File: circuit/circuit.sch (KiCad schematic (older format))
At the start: 4 parts

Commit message: Minor changes
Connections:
- wire segments 11 -> 15
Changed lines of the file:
@@
 EESchema Schematic File Version 4
+LIBS:circuit-cache
 EELAYER 26 0
 EELAYER END
@@
 L pspice:R R1
 U 1 1 5A75EF1D
-P 4700 2450
-F 0 "R1" H 4768 2496 50  0000 L CNN
-F 1 "R" H 4768 2405 50  0000 L CNN
-F 2 "" H 4700 2450 50  0001 C CNN
-F 3 "" H 4700 2450 50  0001 C CNN
-	1    4700 2450
+P 4900 3250
+F 0 "R1" H 4968 3296 50  0000 L CNN
+F 1 "R" H 4968 3205 50  0000 L CNN
+F 2 "" H 4900 3250 50  0001 C CNN
+F 3 "" H 4900 3250 50  0001 C CNN
+	1    4900 3250
 	1    0    0    -1
 $EndComp
@@
 L pspice:R R2
 U 1 1 5A75EF72
-P 5150 2450
-F 0 "R2" H 5218 2496 50  0000 L CNN
-F 1 "R" H 5218 2405 50  0000 L CNN
-F 2 "" H 5150 2450 50  0001 C CNN
-F 3 "" H 5150 2450 50  0001 C CNN
-	1    5150 2450
+P 5350 3250
+F 0 "R2" H 5418 3296 50  0000 L CNN
+F 1 "R" H 5418 3205 50  0000 L CNN
+F 2 "" H 5350 3250 50  0001 C CNN
+F 3 "" H 5350 3250 50  0001 C CNN
+	1    5350 3250
 	1    0    0    -1
 $EndComp
@@
 L pspice:R R3
 U 1 1 5A75F004
-P 5650 2450
-F 0 "R3" H 5718 2496 50  0000 L CNN
-F 1 "R" H 5718 2405 50  0000 L CNN
-F 2 "" H 5650 2450 50  0001 C CNN
-F 3 "" H 5650 2450 50  0001 C CNN
-	1    5650 2450
+P 5850 3250
+F 0 "R3" H 5918 3296 50  0000 L CNN
+F 1 "R" H 5918 3205 50  0000 L CNN
+F 2 "" H 5850 3250 50  0001 C CNN
+F 3 "" H 5850 3250 50  0001 C CNN
+	1    5850 3250
 	1    0    0    -1
 $EndComp
@@
 L pspice:R R4
 U 1 1 5A75F069
-P 6200 2450
-F 0 "R4" H 6268 2496 50  0000 L CNN
-F 1 "R" H 6268 2405 50  0000 L CNN
-F 2 "" H 6200 2450 50  0001 C CNN
-F 3 "" H 6200 2450 50  0001 C CNN
-	1    6200 2450
+P 6400 3250
+F 0 "R4" H 6468 3296 50  0000 L CNN
+F 1 "R" H 6468 3205 50  0000 L CNN
+F 2 "" H 6400 3250 50  0001 C CNN
+F 3 "" H 6400 3250 50  0001 C CNN
+	1    6400 3250
 	1    0    0    -1
 $EndComp
 Wire Wire Line
-	4700 2150 4700 2200
+	4900 2950 4900 3000
 Wire Wire Line
-	4700 2150 5150 2150
+	5350 2950 5350 3000
 Wire Wire Line
-	5150 2150 5150 2200
+	5850 2950 5850 3000
 Wire Wire Line
-	5150 2150 5650 2150
-Wire Wire Line
-	5650 2150 5650 2200
-Connection ~ 5150 2150
-Wire Wire Line
-	5650 2150 6200 2150
-Wire Wire Line
-	6200 2150 6200 2200
-Connection ~ 5650 2150
+	6400 2950 6400 3000
 $Comp
 L power:GND #PWR01
 U 1 1 5A75F0E8
-P 6200 2800
-F 0 "#PWR01" H 6200 2550 50  0001 C CNN
-F 1 "GND" H 6205 2627 50  0000 C CNN
-F 2 "" H 6200 2800 50  0001 C CNN
-F 3 "" H 6200 2800 50  0001 C CNN
-	1    6200 2800
+P 6400 3600
+F 0 "#PWR01" H 6400 3350 50  0001 C CNN
+F 1 "GND" H 6405 3427 50  0000 C CNN
+F 2 "" H 6400 3600 50  0001 C CNN
+F 3 "" H 6400 3600 50  0001 C CNN
+	1    6400 3600
 	1    0    0    -1
 $EndComp
 Wire Wire Line
-	6200 2800 6200 2700
+	6400 3600 6400 3500
 $Comp
 L power:GND #PWR02
 U 1 1 5A75F133
-P 5650 2800
-F 0 "#PWR02" H 5650 2550 50  0001 C CNN
-F 1 "GND" H 5655 2627 50  0000 C CNN
-F 2 "" H 5650 2800 50  0001 C CNN
-F 3 "" H 5650 2800 50  0001 C CNN
-	1    5650 2800
+P 5850 3600
+F 0 "#PWR02" H 5850 3350 50  0001 C CNN
+F 1 "GND" H 5855 3427 50  0000 C CNN
+F 2 "" H 5850 3600 50  0001 C CNN
+F 3 "" H 5850 3600 50  0001 C CNN
+	1    5850 3600
 	1    0    0    -1
 $EndComp
 Wire Wire Line
-	5650 2800 5650 2700
+	5850 3600 5850 3500
 $Comp
 L power:GND #PWR03
 U 1 1 5A75F178
-P 5150 2800
-F 0 "#PWR03" H 5150 2550 50  0001 C CNN
-F 1 "GND" H 5155 2627 50  0000 C CNN
-F 2 "" H 5150 2800 50  0001 C CNN
-F 3 "" H 5150 2800 50  0001 C CNN
-	1    5150 2800
+P 5350 3600
+F 0 "#PWR03" H 5350 3350 50  0001 C CNN
+F 1 "GND" H 5355 3427 50  0000 C CNN
+F 2 "" H 5350 3600 50  0001 C CNN
+F 3 "" H 5350 3600 50  0001 C CNN
+	1    5350 3600
 	1    0    0    -1
 $EndComp
 Wire Wire Line
-	5150 2800 5150 2700
+	5350 3600 5350 3500
 $Comp
 L power:GND #PWR04
 U 1 1 5A75F1DB
-P 4700 2800
-F 0 "#PWR04" H 4700 2550 50  0001 C CNN
-F 1 "GND" H 4705 2627 50  0000 C CNN
-F 2 "" H 4700 2800 50  0001 C CNN
-F 3 "" H 4700 2800 50  0001 C CNN
-	1    4700 2800
+P 4900 3600
+F 0 "#PWR04" H 4900 3350 50  0001 C CNN
+F 1 "GND" H 4905 3427 50  0000 C CNN
+F 2 "" H 4900 3600 50  0001 C CNN
+F 3 "" H 4900 3600 50  0001 C CNN
+	1    4900 3600
 	1    0    0    -1
 $EndComp
 Wire Wire Line
-	4700 2800 4700 2700
+	4900 3600 4900 3500
+Wire Wire Line
+	5850 2950 6150 2950
+Wire Wire Line
+	5350 2950 5100 2950
+Wire Wire Line
+	5100 2950 5100 2650
+Wire Wire Line
+	5100 2650 6150 2650
+Wire Wire Line
+	6150 2650 6150 2950
+Connection ~ 5100 2950
+Wire Wire Line
+	5100 2950 4900 2950
+Connection ~ 6150 2950
+Wire Wire Line
+	6150 2950 6400 2950
 $EndSCHEMATC

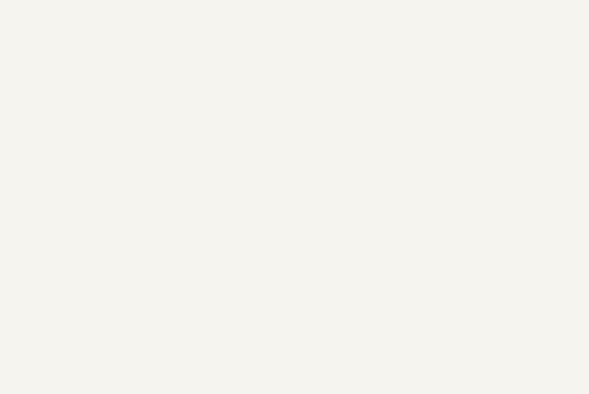
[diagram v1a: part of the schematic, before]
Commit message: Add resistor on misc
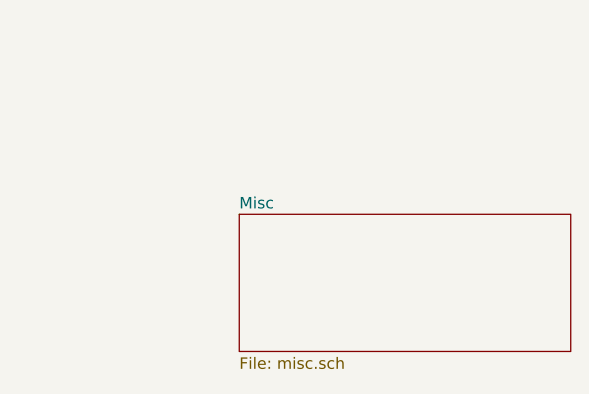
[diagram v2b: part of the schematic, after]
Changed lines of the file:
@@
 $Descr A4 11693 8268
 encoding utf-8
-Sheet 1 1
+Sheet 1 2
 Title ""
 Date ""
@@
 Wire Wire Line
 	6150 2950 6400 2950
+$Sheet
+S 8200 3750 1450 600
+U 5A75F271
+F0 "Misc" 50
+F1 "misc.sch" 50
+$EndSheet
 $EndSCHEMATC

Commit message: last changes
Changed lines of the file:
@@
 	6150 2950 6400 2950
 $Sheet
-S 8200 3750 1450 600
+S 4900 4200 1450 600
 U 5A75F271
 F0 "Misc" 50
